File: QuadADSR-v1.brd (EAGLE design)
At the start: 66.6 x 100 mm, 75 parts, among them IC1 74AC32D, IC5 MCP6004D, Q1 20MHz, T1 2N3904, T2 2N3904, T3 2N3904, T4 2N3904, U1 ATMEGA328P, U2 DUAL_OPAMP, U3 7805, U4 4051

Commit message: using GMSN! output table
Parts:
- removed CV1, CV2, CV3, CV4: S_JACK, INSTRUO:S_JACK
- removed IC5: MCP6004D, GMSN-R2Project:SO14
- added BUT1, BUT2, BUT3, BUT4: PB6149L-5, INSTRUO:PB6149L
- added C18, C20, C22, C3: 560p, rcl:C0805K
- added C19, C21, C23, C6: 47p, rcl:C0805K
- added IC2, IC3: TL074D, linear:SO14
- added OUTPUT1, OUTPUT2, OUTPUT3, OUTPUT4: (no value), INSTRUO:S_JACK
- added R20, R22, R25, R27, R30, R32, R35, R37: 56k, rcl:R0805
- added R21, R26, R31, R36: 30K, rcl:R0805
- added R23, R28, R33, R38: 330R, rcl:R0805
- added R24, R29, R34, R39: 1K, rcl:R0805
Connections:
- removed net N$13: CV1.TIP, IC5.8, IC5.9
- removed net N$25: CV4.TIP, IC5.6, IC5.7
- removed net N$31: CV3.TIP, IC5.1, IC5.2
- removed net N$36: CV2.TIP, IC5.13, IC5.14
- new net N$16: C3.1, IC2.10, IC2.12, R20.2
- new net N$17: C6.1, IC2.9, R21.1, R22.2
- new net N$23: OUTPUT2.TIP, R21.2, R24.2
- new net N$24: BUT2.A, IC2.13, IC2.14
- new net N$26: BUT2.K, R23.1
- new net N$27: C6.2, IC2.8, R24.1
- new net N$28: C18.1, IC2.3, IC2.5, R25.2
- new net N$29: C19.1, IC2.2, R26.1, R27.2
- new net N$30: OUTPUT1.TIP, R26.2, R29.2
- new net N$32: BUT1.A, IC2.6, IC2.7
- new net N$33: BUT1.K, R28.1
- new net N$34: C19.2, IC2.1, R29.1
- new net N$35: R25.1
- new net N$37: R20.1
- new net N$38: C20.1, IC3.3, IC3.5, R30.2
- new net N$39: C21.1, IC3.2, R31.1, R32.2
- new net N$40: OUTPUT3.TIP, R31.2, R34.2
- new net N$41: BUT3.A, IC3.6, IC3.7
- new net N$42: BUT3.K, R33.1
- new net N$43: C21.2, IC3.1, R34.1
- new net N$44: R30.1
- new net N$45: C22.1, IC3.10, IC3.12, R35.2
- new net N$46: C23.1, IC3.9, R36.1, R37.2
- new net N$47: OUTPUT4.TIP, R36.2, R39.2
- new net N$48: BUT4.A, IC3.13, IC3.14
- new net N$49: BUT4.K, R38.1
- new net N$50: C23.2, IC3.8, R39.1
- new net N$51: R35.1
- net +5V: now also IC2.4, IC3.4; no longer IC5.4
- net GND: now also C18.2, C20.2, C22.2, C3.2, IC2.11, IC3.11, OUTPUT1.GND, OUTPUT2.GND, OUTPUT3.GND, OUTPUT4.GND, R22.1, R23.2, R27.1, R28.2, R32.1, R33.2, R37.1, R38.2; no longer CV1.GND, CV2.GND, CV3.GND, CV4.GND, IC5.11
- net VOUTA: no longer IC5.10
- net VOUTB: no longer IC5.12
- net VOUTC: no longer IC5.3
- net VOUTD: no longer IC5.5
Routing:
- net N$13: track 67.9 -> 0.00 mm, vias 2 -> 0
- net N$36: track 64.0 -> 0.00 mm, vias 1 -> 0
- net N$31: track 51.2 -> 0.00 mm, vias 1 -> 0
- net N$25: track 36.2 -> 0.00 mm, vias 1 -> 0
- net GND: track 615.4 -> 594.8 mm

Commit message: removed Switch and checked Schmitt
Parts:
- removed BUT1, BUT2, BUT3, BUT4: PB6149L-5, INSTRUO:PB6149L
- removed MODESW: (no value), INSTRUO:TOGGLE_ON_OFF_ON
- removed R10: 1K, rcl:R0805
- removed R11, R12: 100K, rcl:R0805
- removed U2: DUAL_OPAMP, INSTRUO:DUAL_OPAMP
- added C24: 100n, rcl:C0805K
- added C25, C26, C27, C28: 560p, rcl:C0805K
- added IC4: 4093D, 40xx:SO14
- added IC7: 74AC00D, 74xx-eu:SO14
- added R40, R42: 10K, rcl:R0805
- added R41, R43: 1K, rcl:R0805
- IC1: value 74AC32D -> 4093D; device 74xx-eu:SO14 -> 40xx:SO14
- R17, R19: value (none) -> 1K; device resistor:R0805 -> rcl:R0805
- R18, R9: value (none) -> 10K; device resistor:R0805 -> rcl:R0805
- moved R38 356.7 mm to (44.5, 114.3)
- moved IC3 335.0 mm to (45.7, 77.6), turned to 180 degrees
- moved R37 321.6 mm to (35.6, 73.7)
- moved R33 321.0 mm to (50.8, 114.3)
- moved R39 316.4 mm to (40.6, 68.6)
- moved C23 315.3 mm to (35.6, 68.6)
- moved R36 310.2 mm to (48.3, 68.6)
- moved R35 308.6 mm to (58.4, 64.8)
- moved R34 296.2 mm to (40.6, 85.1)
- moved OUTPUT4 294.9 mm to (45.5, 72.7), flipped to the bottom, turned to 270 degrees
- moved R32 290.3 mm to (38.1, 78.7)
- moved R31 290.0 mm to (48.3, 85.1)
- moved R30 289.4 mm to (35.6, 85.1)
- moved C21 288.6 mm to (33.0, 78.7)
- moved C3 287.0 mm to (19.1, 114.3)
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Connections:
- removed net LED_A: R9.2, U1.30
- removed net LED_B: R17.2, U1.31
- removed net LED_C: R18.2, U1.1
- removed net LED_D: R19.2, U1.2
- removed net N$12: MODESW.2, R10.1
- removed net N$21: D5.A, R18.1
- removed net N$37: R20.1
- removed net T1: MODESW.3, R11.2, U1.10
- removed net T2: MODESW.1, R12.2, U1.11
- new net N$31: C26.1, IC1.11
- new net N$36: IC4.3, R41.1
- new net N$52: IC1.4, R43.1
- new net N$54: C28.1, IC4.4
- new net PULSE1: IC7.1, R17.2
- new net PULSE2: IC7.2, R19.2
- new net PULSE3: IC7.4, R41.2
- new net PULSE4: IC7.5, R43.2
- net +12V: now also C15.1, IC2.4, IC3.4; no longer U2.+VCC
- net +5V: now also IC4.14, IC7.14; no longer C15.1, IC2.4, IC3.4, R10.2
- net -12V: now also C24.2, IC2.11, IC3.11; no longer U2.-VCC
- net GND: now also C24.1, IC4.7, IC7.7, R18.1, R40.1, R42.1, R9.1; no longer D3.K, D4.K, D5.K, D6.K, IC2.11, IC3.11, R11.1, R12.1
- net N$11: now also C26.2, IC1.9, R18.2; no longer IC1.2
- net N$14: now also IC1.10, R19.1; no longer IC1.1, IC1.6
- net N$19: now also C25.2, IC4.8, IC4.9, R9.2; no longer D3.A, R9.1
- net N$20: now also IC4.10; no longer D4.A
- net N$22: now also C25.1, IC4.11; no longer D6.A, R19.1
- net N$24: now also D4.A; no longer BUT2.A
- net N$26: now also D4.K; no longer BUT2.K
- net N$32: now also D3.A; no longer BUT1.A
- net N$33: now also D3.K; no longer BUT1.K
- net N$35: now also C27.2, IC4.1, IC4.2, R40.2; no longer R25.1
- net N$41: now also D5.A; no longer BUT3.A
- net N$42: now also D5.K; no longer BUT3.K
- net N$44: now also C27.1, IC1.3; no longer R30.1
- net N$48: now also D6.A; no longer BUT4.A
- net N$49: now also D6.K; no longer BUT4.K
- net N$51: now also C28.2, IC1.5, IC1.6, R42.2; no longer R35.1
- net TRIG: now also IC7.3; no longer IC1.3
- net TRIG1: now also IC4.12, IC4.13; no longer IC1.10
- net TRIG2: now also IC1.12, IC1.13, IC7.6, U1.1; no longer IC1.9
- net TRIG3: now also IC1.1, IC1.2; no longer IC1.5
- net TRIG4: now also IC4.5, IC4.6; no longer IC1.4
- net VOUTA: now also R25.1
- net VOUTB: now also R20.1
- net VOUTC: now also R30.1
- net VOUTD: now also R35.1
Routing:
- net GND: track 594.8 -> 0.00 mm, vias 16 -> 0
- net +5V: track 400.4 -> 0.00 mm, vias 10 -> 0
- net TRIG1: track 162.2 -> 0.00 mm, vias 5 -> 0
- net TRIG3: track 155.0 -> 0.00 mm, vias 4 -> 0
- net T2: track 148.1 -> 0.00 mm, vias 5 -> 0
- net TRIG2: track 143.2 -> 0.00 mm, vias 6 -> 0
- net N$18: track 138.7 -> 0.00 mm
- net +12V: track 138.5 -> 0.00 mm, vias 3 -> 0
- net CS1: track 133.8 -> 0.00 mm, vias 6 -> 0
- net TRIG4: track 125.1 -> 0.00 mm, vias 7 -> 0
- net N$12: track 114.1 -> 0.00 mm, vias 3 -> 0
- net MOSI: track 107.2 -> 0.00 mm, vias 4 -> 0
- net TRIG: track 104.2 -> 0.00 mm, vias 2 -> 0
- net T1: track 103.1 -> 0.00 mm, vias 9 -> 0
- net POT_ST: track 101.5 -> 0.00 mm
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
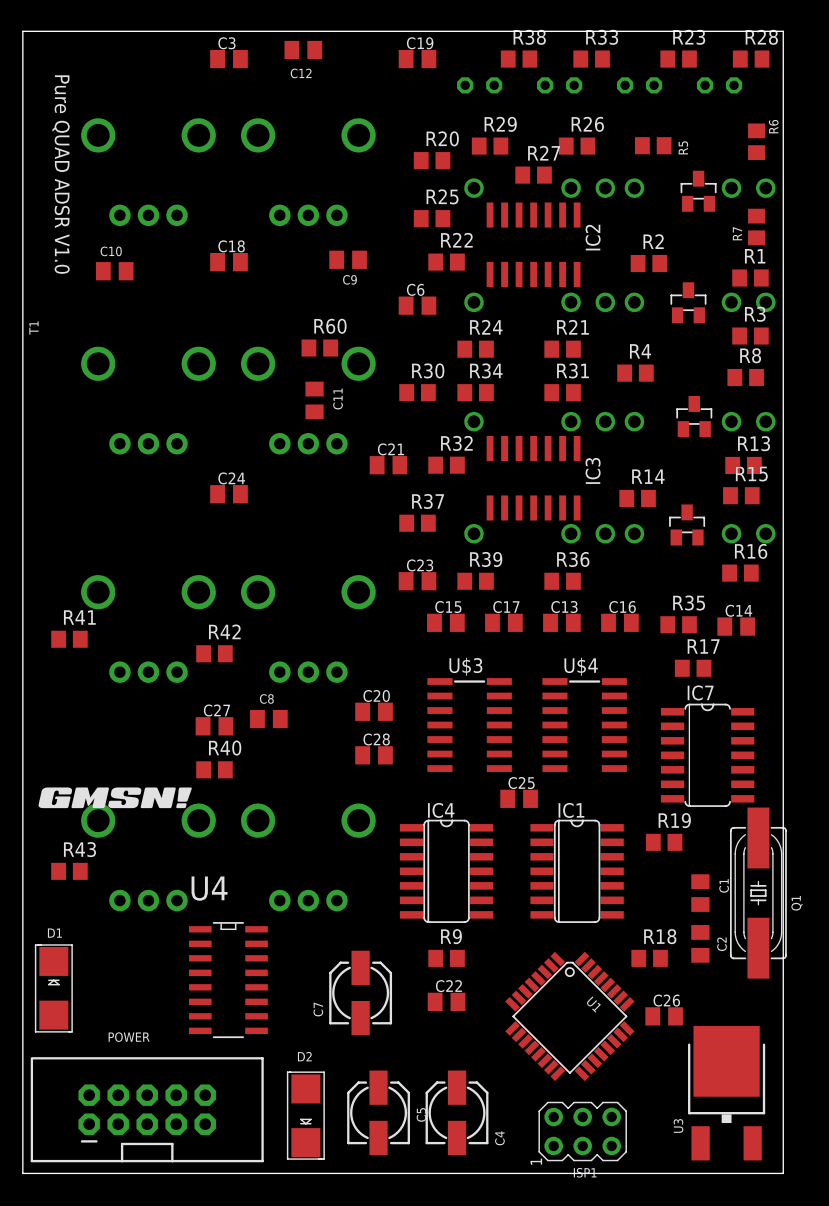
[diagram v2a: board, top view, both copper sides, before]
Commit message: removed Switch and checked Schmitt
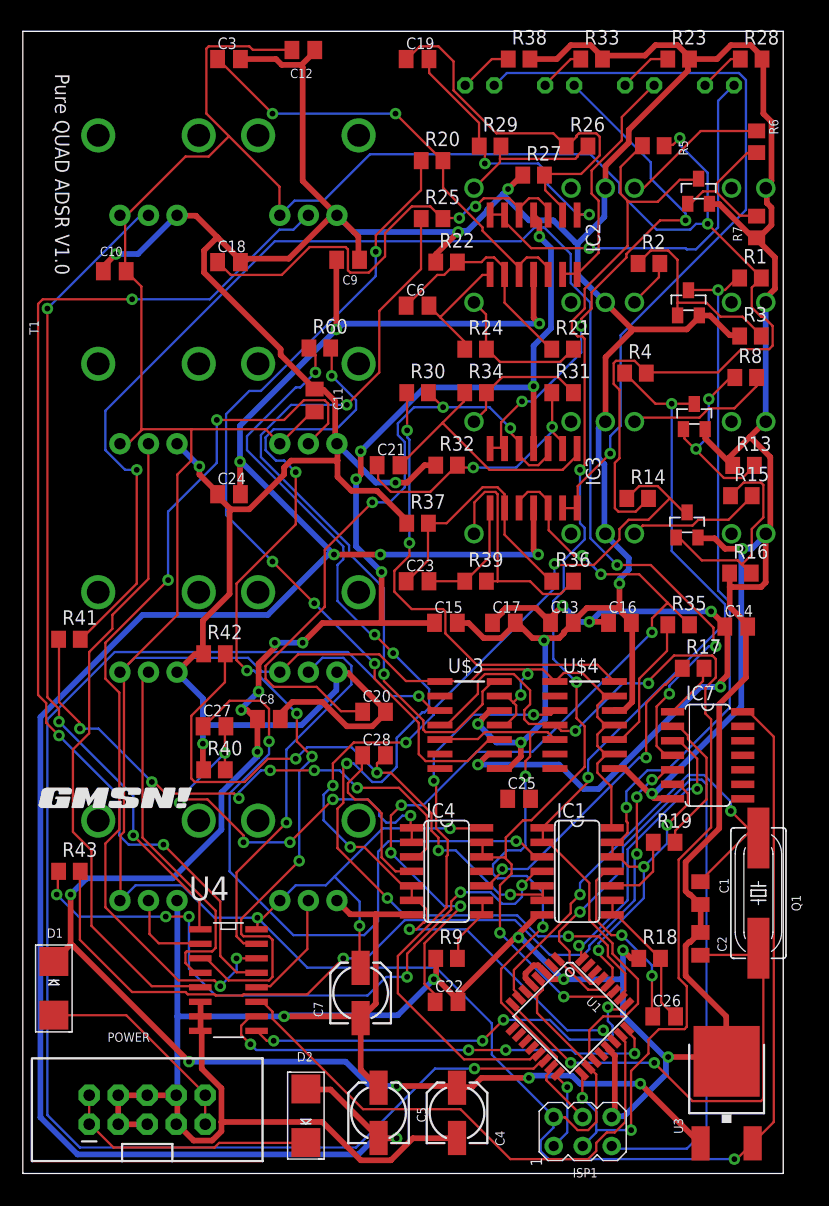
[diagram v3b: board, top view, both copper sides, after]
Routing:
- net GND: track 0.00 -> 686.3 mm, vias 0 -> 18
- net +5V: track 0.00 -> 458.2 mm, vias 0 -> 8
- net -12V: track 0.00 -> 189.9 mm, vias 0 -> 7
- net +12V: track 0.00 -> 175.1 mm, vias 0 -> 15
- net PULSE3: track 0.00 -> 126.5 mm, vias 0 -> 4
- net CS1: track 0.00 -> 121.5 mm, vias 0 -> 2
- net TRIG1: track 0.00 -> 102.4 mm, vias 0 -> 4
- net POT_A: track 0.00 -> 96.2 mm, vias 0 -> 3
- net AIN: track 0.00 -> 94.1 mm, vias 0 -> 6
- net TRIG2: track 0.00 -> 91.8 mm, vias 0 -> 5
- net TRIG4: track 0.00 -> 91.1 mm, vias 0 -> 6
- net SCK: track 0.00 -> 91.0 mm, vias 0 -> 4
- net N$69: track 0.00 -> 81.5 mm, vias 0 -> 6
- net TRIG3: track 0.00 -> 80.4 mm, vias 0 -> 2
- net POT_D: track 0.00 -> 80.2 mm, vias 0 -> 4
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
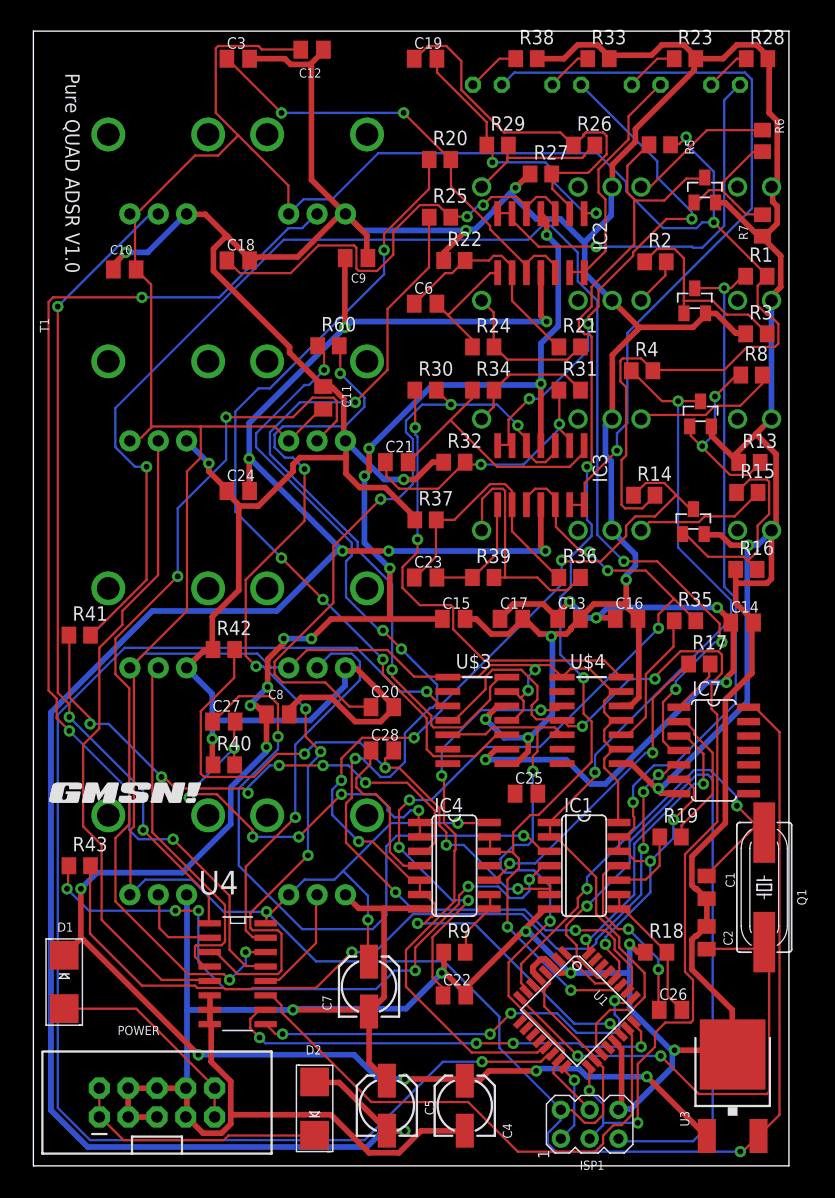
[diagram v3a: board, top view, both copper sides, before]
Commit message: Quad Transistor
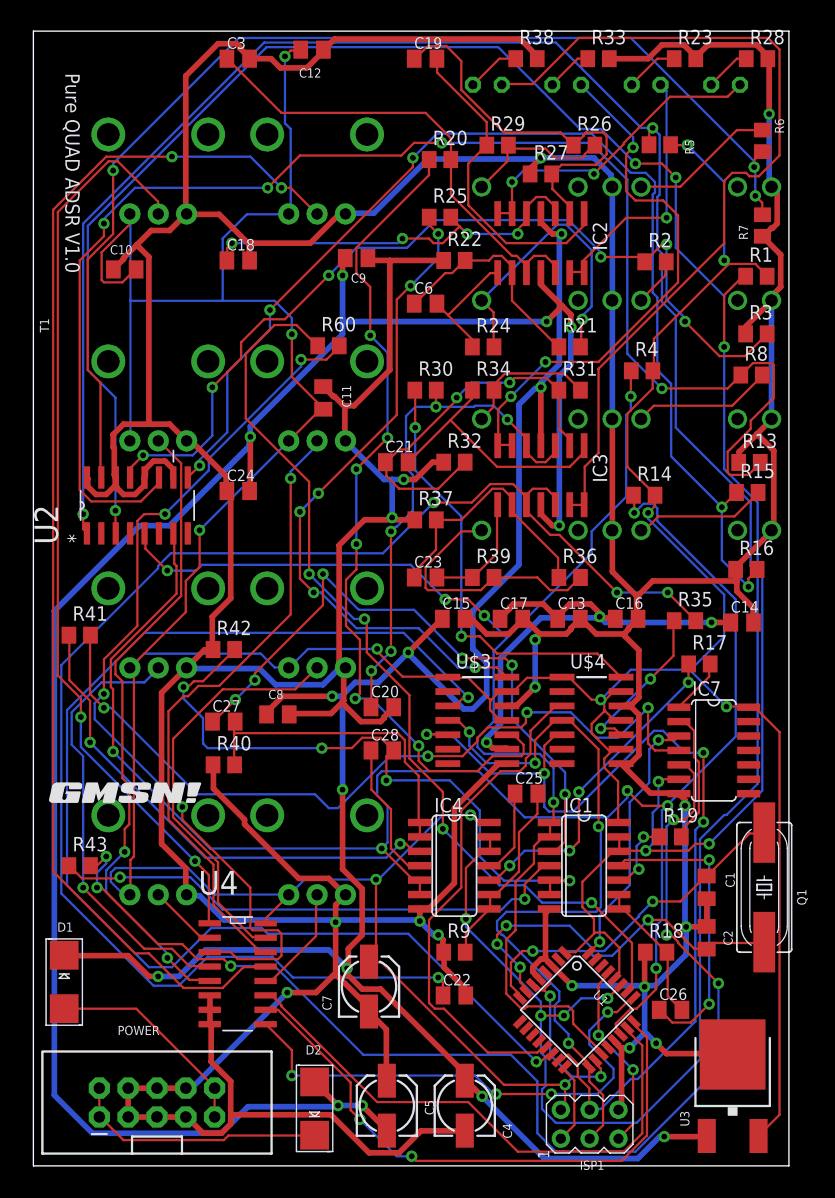
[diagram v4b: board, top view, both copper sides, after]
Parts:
- removed T1, T2, T3, T4: 2N3904, INSTRUO:TRANSISTOR_SINGLE_N-TYPE
- added U2: MMPQ2222A, Fairchild_By_element14_Batch_1:SOIC127P600X175-16N
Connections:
- removed net N$15: R6.1, R7.2, T1.B
- removed net N$3: R2.1, R3.2, T2.B
- removed net N$5: R13.2, R8.1, T3.B
- removed net N$7: R15.1, R16.2, T4.B
- new net B1: R6.1, R7.2, U2.15
- new net B2: R2.1, R3.2, U2.13
- new net B3: R13.2, R8.1, U2.11
- new net B4: R15.1, R16.2, U2.9
- net GND: now also U2.10, U2.12, U2.14, U2.16; no longer T1.E, T2.E, T3.E, T4.E
- net TRIG1: now also U2.1; no longer T1.C
- net TRIG2: now also U2.3; no longer T2.C
- net TRIG3: now also U2.5; no longer T3.C
- net TRIG4: now also U2.7; no longer T4.C
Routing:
- net B3: track 0.00 -> 128.7 mm, vias 0 -> 4
- net TRIG1: track 102.4 -> 230.5 mm, vias 4 -> 6
- net TRIG2: track 91.8 -> 198.5 mm, vias 5 -> 7
- net B4: track 0.00 -> 103.3 mm, vias 0 -> 5
- net B1: track 0.00 -> 101.4 mm, vias 0 -> 3
- net B2: track 0.00 -> 79.7 mm, vias 0 -> 6
- net TRIG4: track 91.1 -> 149.5 mm
- net N$45: track 76.2 -> 133.2 mm, vias 6 -> 4
- net PULSE3: track 126.5 -> 70.8 mm
- net RST: track 65.9 -> 16.8 mm, vias 1 -> 2
- net +5V: track 458.2 -> 412.3 mm, vias 8 -> 14
- net TRIG3: track 80.4 -> 116.8 mm, vias 2 -> 5
- net PULSE4: track 76.1 -> 106.3 mm, vias 4 -> 6
- net MOSI: track 55.2 -> 82.2 mm, vias 2 -> 4
- net POT_D: track 80.2 -> 55.6 mm, vias 4 -> 1
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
